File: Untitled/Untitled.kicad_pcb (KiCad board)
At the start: 2 copper layers, 74.3 x 69.9 mm, 67 parts, among them IC1 DRV8210, IC2 TPS7A2033, J1 5v in, J10 PROG, J2 Volume, J3 Input, J4 IR, J5 Motor out, J6 Relays, J7 PGA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

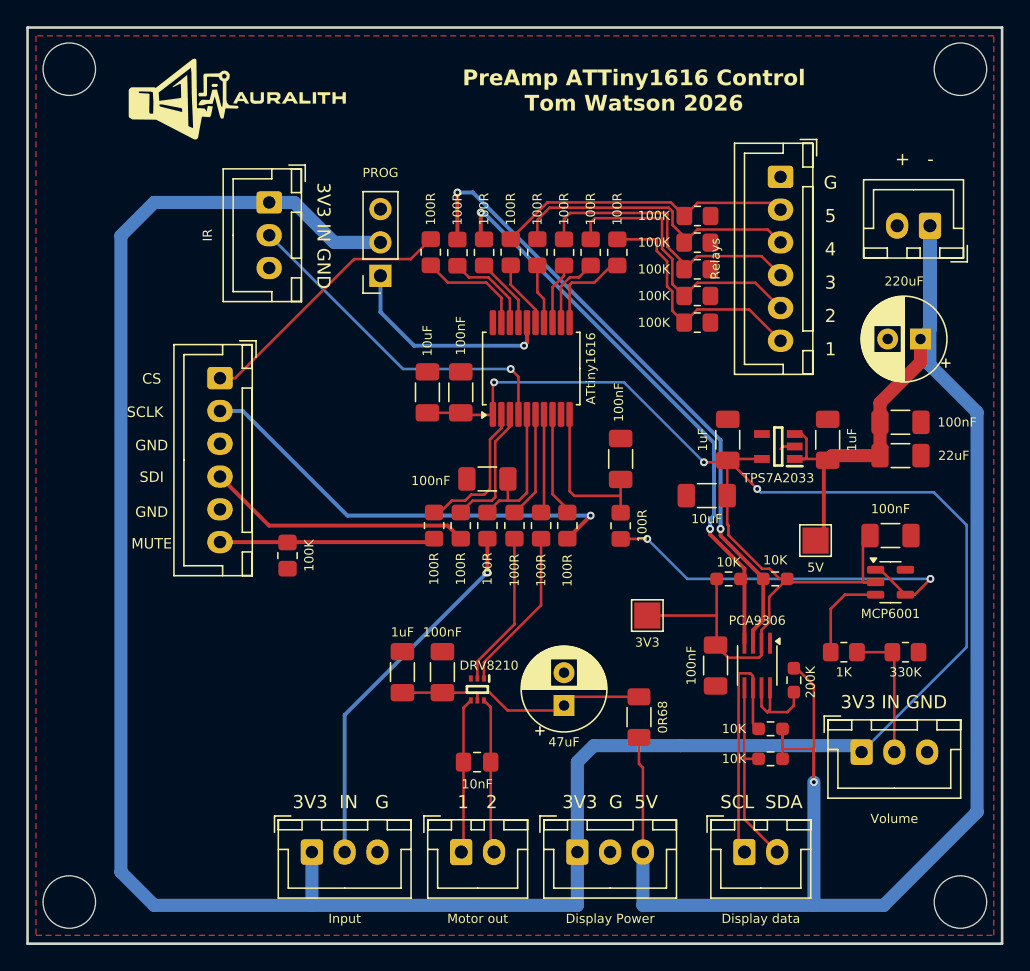
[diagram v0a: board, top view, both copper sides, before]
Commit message: added I2C expander
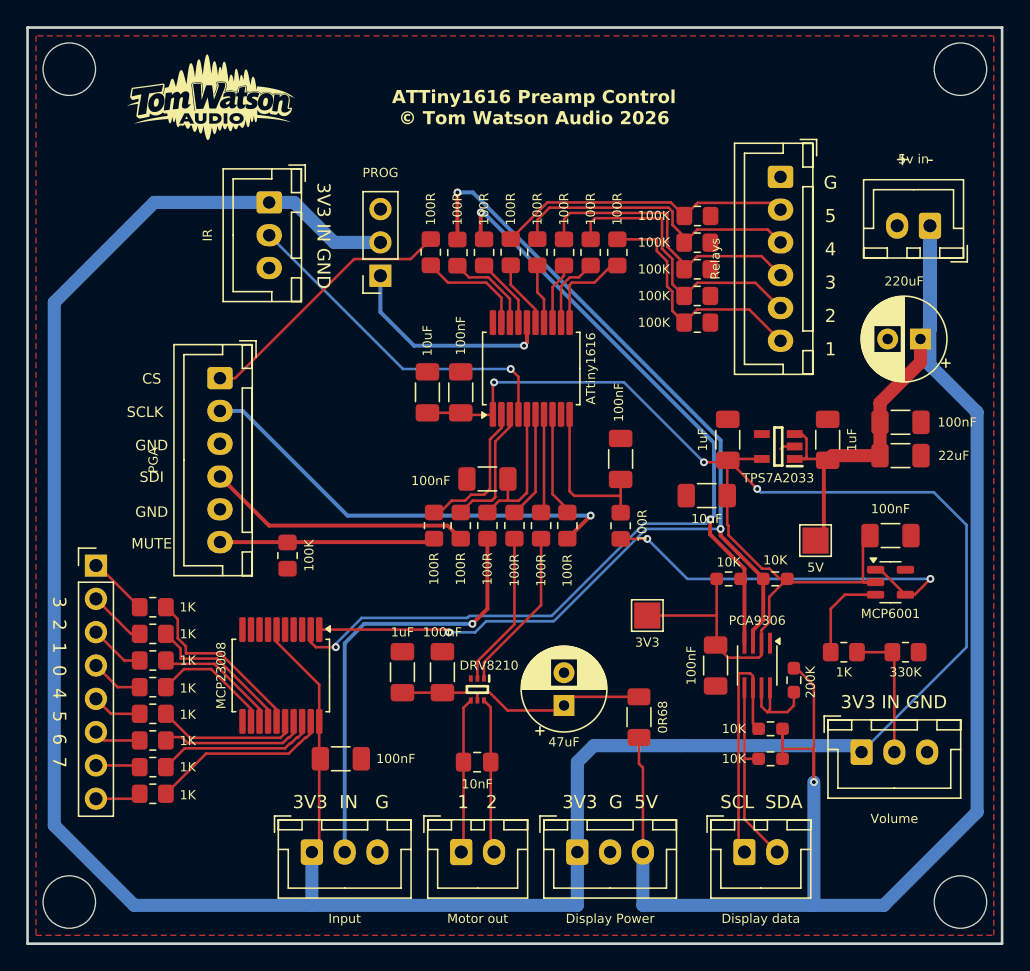
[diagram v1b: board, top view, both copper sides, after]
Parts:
- removed REF**: LOGOTEST, Custom:LOGOTEST
- added C17: 100nF, Capacitor_SMD:C_1206_3216Metric_Pad1.33x1.80mm_HandSolder, F.Cu at (178.8, 119.9)
- added G***: LOGO, Custom:LOGONEW, F.Cu at (168.9, 69.5)
- added J11: Conn_01x08_Socket, Connector_PinHeader_2.54mm:PinHeader_1x08_P2.54mm_Vertical, F.Cu at (160.1, 105.2)
- added R31: 1K, Resistor_SMD:R_0805_2012Metric_Pad1.20x1.40mm_HandSolder, F.Cu at (164.5, 122.6)
- added R32: 1K, Resistor_SMD:R_0805_2012Metric_Pad1.20x1.40mm_HandSolder, F.Cu at (164.5, 120.5)
- added R33: 1K, Resistor_SMD:R_0805_2012Metric_Pad1.20x1.40mm_HandSolder, F.Cu at (164.5, 118.5)
- added R34: 1K, Resistor_SMD:R_0805_2012Metric_Pad1.20x1.40mm_HandSolder, F.Cu at (164.5, 116.5)
- added R35: 1K, Resistor_SMD:R_0805_2012Metric_Pad1.20x1.40mm_HandSolder, F.Cu at (164.5, 114.4)
- added R36: 1K, Resistor_SMD:R_0805_2012Metric_Pad1.20x1.40mm_HandSolder, F.Cu at (164.5, 112.4)
- added R37: 1K, Resistor_SMD:R_0805_2012Metric_Pad1.20x1.40mm_HandSolder, F.Cu at (164.5, 110.4)
- added R38: 1K, Resistor_SMD:R_0805_2012Metric_Pad1.20x1.40mm_HandSolder, F.Cu at (164.5, 108.3)
- added U4: MCP23008, Package_SO:SSOP-20_5.3x7.2mm_P0.65mm, F.Cu at (174.2, 113.5)
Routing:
- net /SDA: track 43.7 -> 79.4 mm, vias 2 -> 3
- net /SCL: track 48.6 -> 82.6 mm, vias 2 -> 3
- net /3V3: track 259.4 -> 283.0 mm
- net Net-(U4-GP7): track 0.00 -> 13.9 mm
- net Net-(U4-GP3): track 0.00 -> 13.7 mm
- net Net-(U4-GP6): track 0.00 -> 12.4 mm
- net Net-(U4-GP2): track 0.00 -> 11.5 mm
- net Net-(U4-GP5): track 0.00 -> 11.2 mm
- net Net-(U4-GP4): track 0.00 -> 10.9 mm
- net Net-(U4-GP1): track 0.00 -> 9.62 mm
- net Net-(U4-GP0): track 0.00 -> 9.27 mm
- net /INPUT-ADC: track 28.4 -> 33.2 mm
- net Net-(J11-Pin_1): track 0.00 -> 4.65 mm
- net Net-(J11-Pin_2): track 0.00 -> 4.44 mm
- net Net-(J11-Pin_3): track 0.00 -> 4.23 mm
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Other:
- board text added: "3 2 1 0 4 5 6 7"
- board text added: "ATTiny1616 Preamp Control © Tom Watson Audio 2026"
- board text removed: "PreAmp ATTiny1616 Control Tom Watson 2026"

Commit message: MCP120-300 additiob
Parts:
- added R39: 10K, Resistor_SMD:R_0805_2012Metric_Pad1.20x1.40mm_HandSolder, F.Cu at (181.9, 86.5)
- added U11: MCP120, Package_TO_SOT_SMD:SOT-23, F.Cu at (181.9, 89.6)
- J1: value 5v in -> POWER
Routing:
- net /3V3: track 283.0 -> 297.5 mm, vias 3 -> 4
- net /PROG: track 16.6 -> 22.7 mm

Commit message: ooo
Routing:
- net /3V3: track 297.5 -> 294.8 mm
- net /5V-IN: track 151.2 -> 149.2 mm
- net /RELAY5: track 23.9 -> 22.1 mm
- net /5V-MOTOR: track 18.8 -> 17.8 mm
- net Net-(U1-PC2): track 5.30 -> 4.58 mm
- net /SCL5V: track 19.2 -> 18.6 mm
- net Net-(J11-Pin_8): track 3.49 -> 2.95 mm
- net /PROG: track 22.7 -> 22.2 mm
